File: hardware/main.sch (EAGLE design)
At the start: 95 parts, among them IC1 MPU-6050, IC2 TB6612FNG, M1 MOTOR_MOUNT_V2, M2 LED_MOUNT, M3 LED_MOUNT, M4 LED_MOUNT, M5 LED_MOUNT, M6 LED_MOUNT, M7 LED_MOUNT, Q7 IRLML2244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

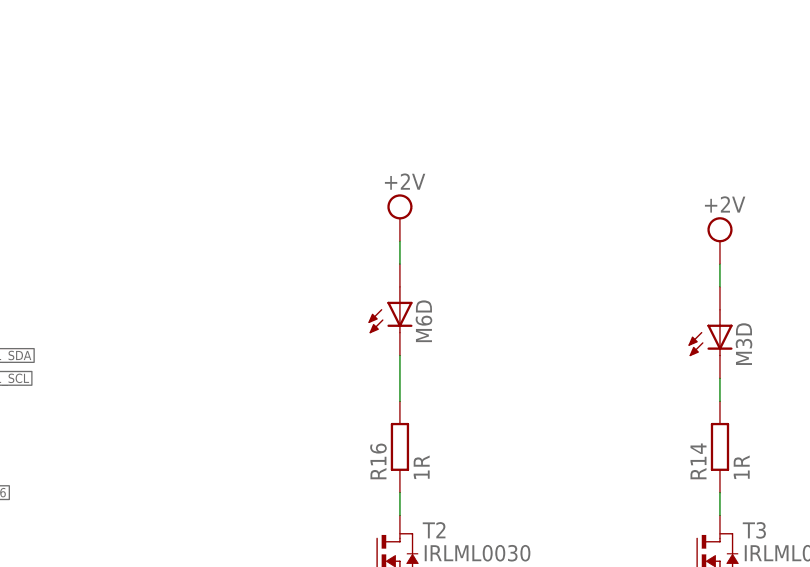
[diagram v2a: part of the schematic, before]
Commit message: led resistors changed to 0603, fixed gnd plane
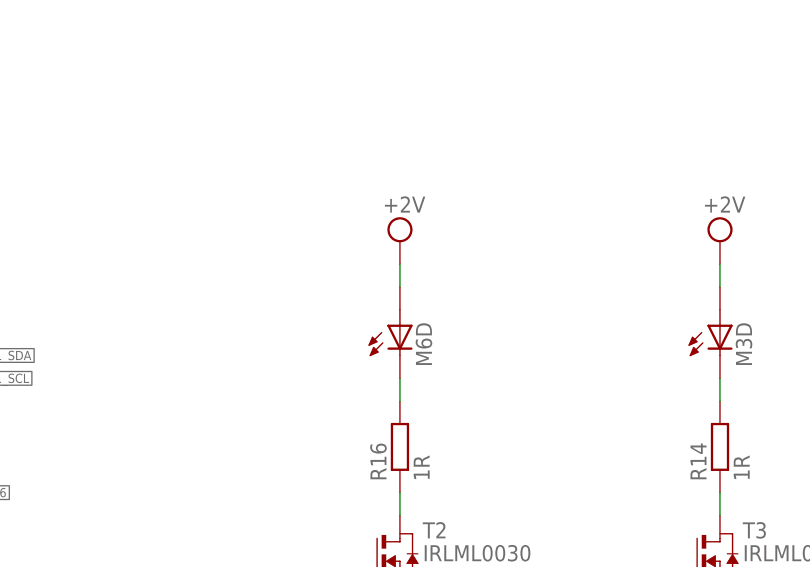
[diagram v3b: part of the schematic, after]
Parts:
- R22, R25, R26, R27, R28, R29, R32: device resistor:R-EU_R0805 -> resistor:R-EU_R0603
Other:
- moved on the sheet: M6D

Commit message: polygons fix
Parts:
- added U$1: GND_CONN, micromouse:GND_CONN
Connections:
- net GND: now also U$1.AGND
- net GNDA: now also U$1.GND
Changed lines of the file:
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@@
 <part name="L1" library="micromouse" deviceset="LABITYNT" device=""/>
 <part name="AGND36" library="supply2" deviceset="GND" device=""/>
+<part name="GND2" library="supply1" deviceset="GNDA" device="" value="GNDM"/>
+<part name="U$1" library="micromouse" deviceset="GND_CONN" device=""/>
 </parts>
 <sheets>
@@
 <instance part="L1" gate="A" x="243.84" y="292.1"/>
 <instance part="AGND36" gate="GND" x="45.72" y="96.52"/>
+<instance part="GND2" gate="1" x="-66.04" y="12.7"/>
+<instance part="U$1" gate="G$1" x="-66.04" y="20.32" rot="R270"/>
 </instances>
 <busses>
@@
 <wire x1="45.72" y1="101.6" x2="45.72" y2="99.06" width="0.1524" layer="91"/>
 <pinref part="AGND36" gate="GND" pin="GND"/>
+</segment>
+<segment>
+<pinref part="U$14" gate="G$1" pin="AGND"/>
+<wire x1="-71.12" y1="25.4" x2="-71.12" y2="27.94" width="0.1524" layer="91"/>
+<pinref part="AGND1" gate="GND" pin="GND"/>
+<wire x1="-71.12" y1="27.94" x2="-66.04" y2="27.94" width="0.1524" layer="91"/>
+<wire x1="-66.04" y1="27.94" x2="-60.96" y2="27.94" width="0.1524" layer="91"/>
+<wire x1="-60.96" y1="27.94" x2="-60.96" y2="25.4" width="0.1524" layer="91"/>
+<junction x="-66.04" y="27.94"/>
+<pinref part="U$1" gate="G$1" pin="AGND"/>
+<wire x1="-66.04" y1="22.86" x2="-66.04" y2="27.94" width="0.1524" layer="91"/>
 </segment>
 </net>
@@
 <junction x="96.52" y="330.2"/>
 <pinref part="D9" gate="G$1" pin="A"/>
+</segment>
+<segment>
+<pinref part="GND2" gate="1" pin="GNDA"/>
+<pinref part="U$1" gate="G$1" pin="GND"/>
+<wire x1="-66.04" y1="15.24" x2="-66.04" y2="17.78" width="0.1524" layer="91"/>
 </segment>
 </net>
@@
 <pinref part="U$13" gate="G$1" pin="AGND"/>
 </segment>
-<segment>
-<pinref part="U$14" gate="G$1" pin="AGND"/>
-<wire x1="-71.12" y1="25.4" x2="-71.12" y2="27.94" width="0.1524" layer="91"/>
-<wire x1="-71.12" y1="27.94" x2="-60.96" y2="27.94" width="0.1524" layer="91"/>
-</segment>
-</net>
+</net>

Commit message: dodanie lini od przerwania od MPU, dodanie C na DCDC 3V3, laczenie GNDA GND i GNDM, dodanie diod ESD na programator, rewizja
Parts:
- removed R18: 1k, rcl:R-EU_R0603
- removed U$1: GND_CONN, micromouse:GND_CONN
- added C2_3: 10u, rcl:C-EUC0805
- added D1: WE-TVS_824015, EAGLE-POWER_MAGNETICS-rev17a:WE-TVS_824015
- added PT1, PT2: 2PT_GND_TIE, SparkFun-Passives:2PT_GND_TIE
- added R6: 1k, rcl:R-EU_R0603
- C4: value 2,2n -> 100nF
- C5: device rcl:C-EUC0603 -> rcl:C-EUC0805
- renumbered U$4 to U2, U$5 to U1, U$6 to U3
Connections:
- removed net N$23: R18.2, R19.2, S1.1
- removed net N$36: IC1.INT
- removed net OSC_OUT: U3.PH1
- new net MPU_INT: IC1.INT, U3.PB7
- new net N$25: R6.2, S4.1
- net +3V3: now also C2_3.1, D1.VDD
- net AGND: now also PT1.P$1
- net BOOT0: now also R19.2, S1.1; no longer R18.1
- net BTN1: now also R6.1; no longer S4.1
- net GND: now also C2_3.2, D1.GND, PT1.P$2, PT2.P$1; no longer U$1.AGND
- net GNDA: now also PT2.P$2; no longer U$1.GND
- net SWCLK: now also D1.3
- net SWDIO: now also D1.4
- net USART3_RX: now also D1.6
- net USART3_TX: now also D1.1
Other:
- note added: "*"
- note added: "Ok"
- note added: "ok"
- moved on the sheet: SV1

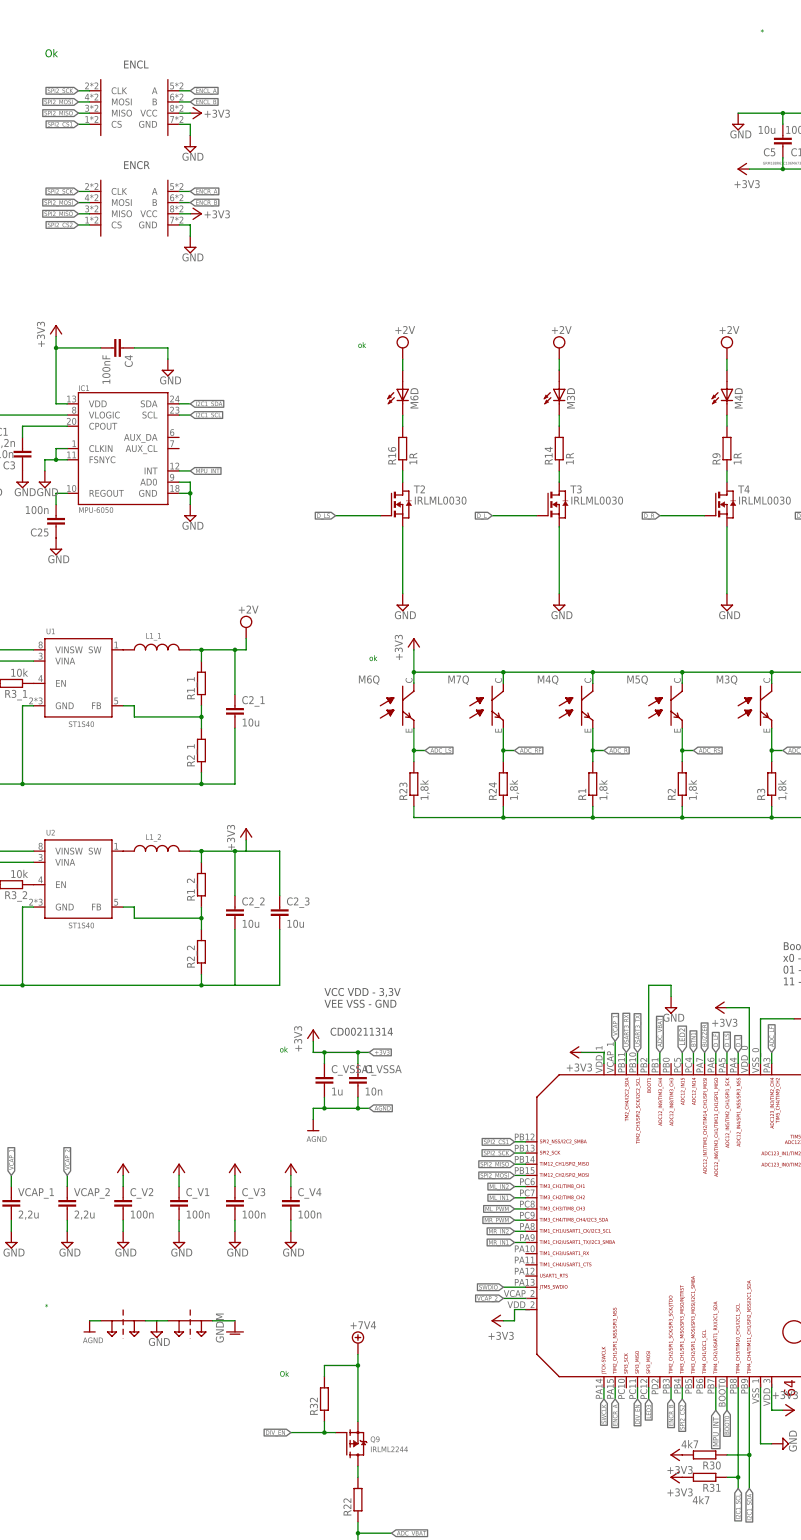
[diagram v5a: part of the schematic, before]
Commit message: encoder lbr fix, connected gnd
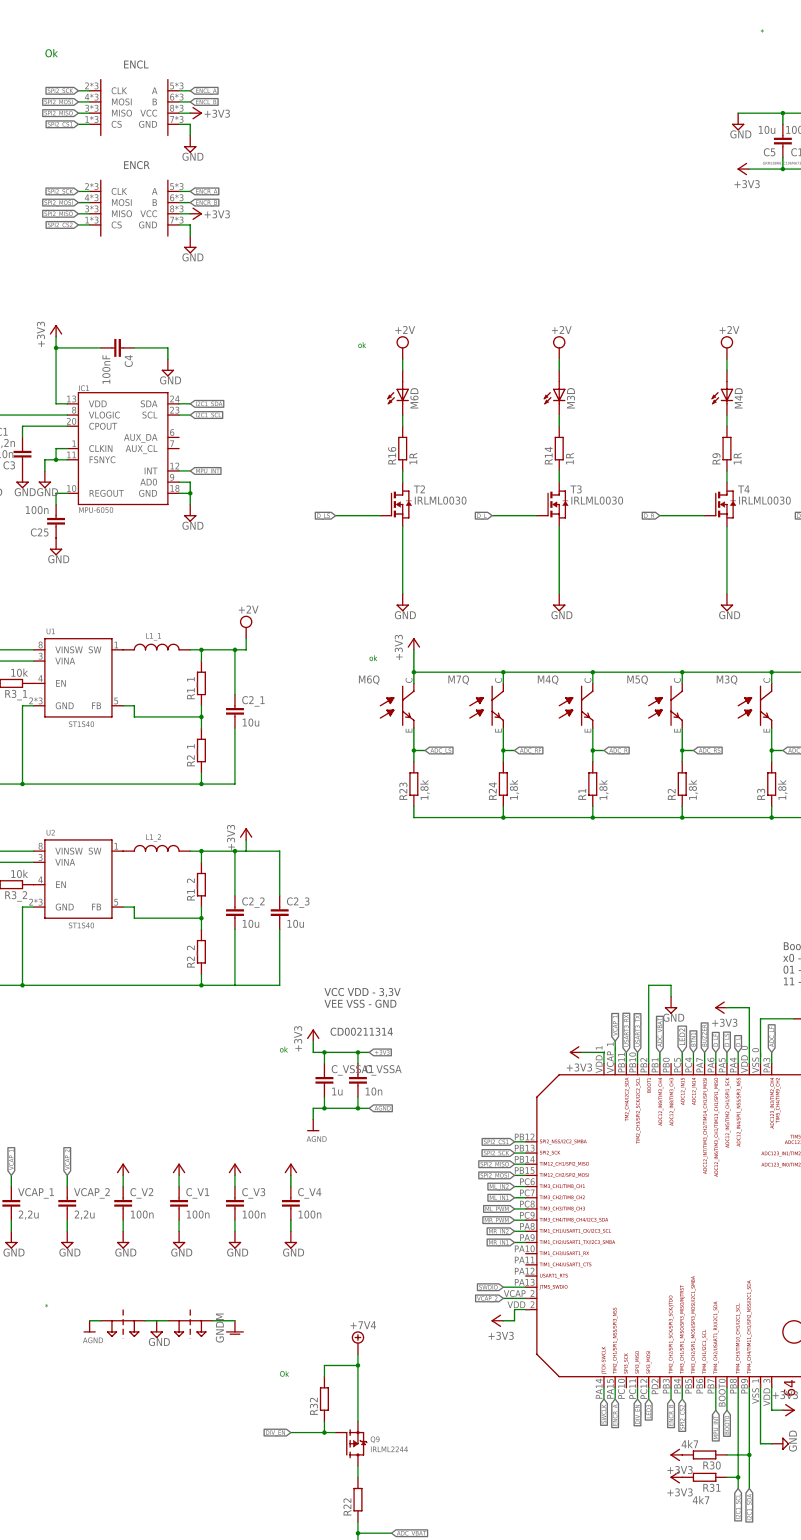
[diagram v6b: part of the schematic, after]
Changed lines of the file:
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@@
 <grid distance="0.1" unitdist="inch" unit="inch" style="lines" multiple="1" display="no" altdistance="0.01" altunitdist="inch" altunit="inch"/>
 <layers>
-<layer number="1" name="Top" color="4" fill="1" visible="yes" active="no"/>
-<layer number="2" name="Route2" color="1" fill="3" visible="yes" active="no"/>
-<layer number="3" name="Route3" color="4" fill="3" visible="yes" active="no"/>
-<layer number="4" name="Route4" color="1" fill="4" visible="yes" active="no"/>
-<layer number="5" name="Route5" color="4" fill="4" visible="yes" active="no"/>
-<layer number="6" name="Route6" color="1" fill="8" visible="yes" active="no"/>
-<layer number="7" name="Route7" color="4" fill="8" visible="yes" active="no"/>
-<layer number="8" name="Route8" color="1" fill="2" visible="yes" active="no"/>
-<layer number="9" name="Route9" color="4" fill="2" visible="yes" active="no"/>
-<layer number="10" name="Route10" color="1" fill="7" visible="yes" active="no"/>
-<layer number="11" name="Route11" color="4" fill="7" visible="yes" active="no"/>
-<layer number="12" name="Route12" color="1" fill="5" visible="yes" active="no"/>
-<layer number="13" name="Route13" color="4" fill="5" visible="yes" active="no"/>
-<layer number="14" name="Route14" color="1" fill="6" visible="yes" active="no"/>
-<layer number="15" name="Route15" color="4" fill="6" visible="yes" active="no"/>
-<layer number="16" name="Bottom" color="1" fill="1" visible="yes" active="no"/>
-<layer number="17" name="Pads" color="2" fill="1" visible="yes" active="no"/>
-<layer number="18" name="Vias" color="2" fill="1" visible="yes" active="no"/>
-<layer number="19" name="Unrouted" color="6" fill="1" visible="yes" active="no"/>
-<layer number="20" name="Dimension" color="15" fill="1" visible="yes" active="no"/>
-<layer number="21" name="tPlace" color="7" fill="1" visible="yes" active="no"/>
-<layer number="22" name="bPlace" color="7" fill="1" visible="yes" active="no"/>
-<layer number="23" name="tOrigins" color="15" fill="1" visible="yes" active="no"/>
-<layer number="24" name="bOrigins" color="15" fill="1" visible="yes" active="no"/>
-<layer number="25" name="tNames" color="7" fill="1" visible="yes" active="no"/>
-<layer number="26" name="bNames" color="7" fill="1" visible="yes" active="no"/>
-<layer number="27" name="tValues" color="7" fill="1" visible="yes" active="no"/>
-<layer number="28" name="bValues" color="7" fill="1" visible="yes" active="no"/>
+<layer number="1" name="Top" color="4" fill="1" visible="no" active="no"/>
+<layer number="2" name="Route2" color="1" fill="3" visible="no" active="no"/>
+<layer number="3" name="Route3" color="4" fill="3" visible="no" active="no"/>
+<layer number="4" name="Route4" color="1" fill="4" visible="no" active="no"/>
+<layer number="5" name="Route5" color="4" fill="4" visible="no" active="no"/>
+<layer number="6" name="Route6" color="1" fill="8" visible="no" active="no"/>
+<layer number="7" name="Route7" color="4" fill="8" visible="no" active="no"/>
+<layer number="8" name="Route8" color="1" fill="2" visible="no" active="no"/>
+<layer number="9" name="Route9" color="4" fill="2" visible="no" active="no"/>
+<layer number="10" name="Route10" color="1" fill="7" visible="no" active="no"/>
+<layer number="11" name="Route11" color="4" fill="7" visible="no" active="no"/>
+<layer number="12" name="Route12" color="1" fill="5" visible="no" active="no"/>
+<layer number="13" name="Route13" color="4" fill="5" visible="no" active="no"/>
+<layer number="14" name="Route14" color="1" fill="6" visible="no" active="no"/>
+<layer number="15" name="Route15" color="4" fill="6" visible="no" active="no"/>
+<layer number="16" name="Bottom" color="1" fill="1" visible="no" active="no"/>
+<layer number="17" name="Pads" color="2" fill="1" visible="no" active="no"/>
+<layer number="18" name="Vias" color="2" fill="1" visible="no" active="no"/>
+<layer number="19" name="Unrouted" color="6" fill="1" visible="no" active="no"/>
+<layer number="20" name="Dimension" color="15" fill="1" visible="no" active="no"/>
+<layer number="21" name="tPlace" color="7" fill="1" visible="no" active="no"/>
+<layer number="22" name="bPlace" color="7" fill="1" visible="no" active="no"/>
+<layer number="23" name="tOrigins" color="15" fill="1" visible="no" active="no"/>
+<layer number="24" name="bOrigins" color="15" fill="1" visible="no" active="no"/>
+<layer number="25" name="tNames" color="7" fill="1" visible="no" active="no"/>
+<layer number="26" name="bNames" color="7" fill="1" visible="no" active="no"/>
+<layer number="27" name="tValues" color="7" fill="1" visible="no" active="no"/>
+<layer number="28" name="bValues" color="7" fill="1" visible="no" active="no"/>
 <layer number="29" name="tStop" color="7" fill="3" visible="no" active="no"/>
 <layer number="30" name="bStop" color="7" fill="6" visible="no" active="no"/>
@@
 <layer number="35" name="tGlue" color="7" fill="4" visible="no" active="no"/>
 <layer number="36" name="bGlue" color="7" fill="5" visible="no" active="no"/>
-<layer number="37" name="tTest" color="7" fill="1" visible="yes" active="no"/>
-<layer number="38" name="bTest" color="7" fill="1" visible="yes" active="no"/>
+<layer number="37" name="tTest" color="7" fill="1" visible="no" active="no"/>
+<layer number="38" name="bTest" color="7" fill="1" visible="no" active="no"/>
 <layer number="39" name="tKeepout" color="4" fill="11" visible="no" active="no"/>
 <layer number="40" name="bKeepout" color="1" fill="11" visible="no" active="no"/>
@@
 <layer number="44" name="Drills" color="7" fill="1" visible="no" active="no"/>
 <layer number="45" name="Holes" color="7" fill="1" visible="no" active="no"/>
-<layer number="46" name="Milling" color="3" fill="1" visible="yes" active="no"/>
-<layer number="47" name="Measures" color="7" fill="1" visible="yes" active="no"/>
-<layer number="48" name="Document" color="7" fill="1" visible="yes" active="no"/>
-<layer number="49" name="Reference" color="7" fill="1" visible="yes" active="no"/>
-<layer number="50" name="dxf" color="7" fill="1" visible="yes" active="no"/>
-<layer number="51" name="tDocu" color="7" fill="1" visible="yes" active="no"/>
-<layer number="52" name="bDocu" color="7" fill="1" visible="yes" active="no"/>
-<layer number="53" name="tGND_GNDA" color="7" fill="9" visible="yes" active="no"/>
-<layer number="54" name="bGND_GNDA" color="1" fill="9" visible="yes" active="no"/>
-<layer number="56" name="wert" color="7" fill="1" visible="yes" active="no"/>
-<layer number="57" name="tCAD" color="7" fill="1" visible="yes" active="no"/>
-<layer number="59" name="tCarbon" color="7" fill="1" visible="yes" active="no"/>
-<layer number="60" name="bCarbon" color="7" fill="1" visible="yes" active="no"/>
+<layer number="46" name="Milling" color="3" fill="1" visible="no" active="no"/>
+<layer number="47" name="Measures" color="7" fill="1" visible="no" active="no"/>
+<layer number="48" name="Document" color="7" fill="1" visible="no" active="no"/>
+<layer number="49" name="Reference" color="7" fill="1" visible="no" active="no"/>
+<layer number="50" name="dxf" color="7" fill="1" visible="no" active="no"/>
+<layer number="51" name="tDocu" color="7" fill="1" visible="no" active="no"/>
+<layer number="52" name="bDocu" color="7" fill="1" visible="no" active="no"/>
+<layer number="53" name="tGND_GNDA" color="7" fill="9" visible="no" active="no"/>
+<layer number="54" name="bGND_GNDA" color="1" fill="9" visible="no" active="no"/>
+<layer number="56" name="wert" color="7" fill="1" visible="no" active="no"/>
+<layer number="57" name="tCAD" color="7" fill="1" visible="no" active="no"/>
+<layer number="59" name="tCarbon" color="7" fill="1" visible="no" active="no"/>
+<layer number="60" name="bCarbon" color="7" fill="1" visible="no" active="no"/>
 <layer number="90" name="Modules" color="5" fill="1" visible="yes" active="yes"/>
 <layer number="91" name="Nets" color="2" fill="1" visible="yes" active="yes"/>
@@
 <pinref part="U3" gate="G$1" pin="PB7"/>
 <wire x1="55.88" y1="10.16" x2="55.88" y2="5.08" width="0.1524" layer="91"/>
-<label x="55.88" y="5.08" size="1.27" layer="95" rot="R270" xref="yes"/>
-</segment>
-<segment>
+<label x="55.88" y="5.08" size="1.016" layer="95" rot="R270" xref="yes"/>
+</segment>
+<segment>
